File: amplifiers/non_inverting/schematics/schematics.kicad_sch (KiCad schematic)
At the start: 5 parts, among them J1 15V, U1 LM741

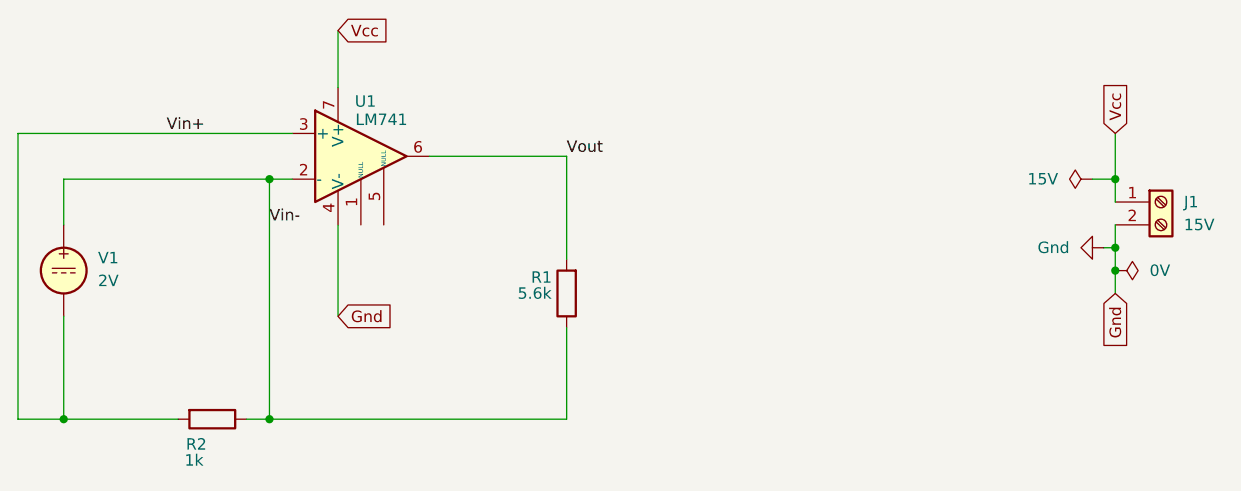
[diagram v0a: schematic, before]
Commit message: docs: update schematics.prl files for inverting and non-inverting amplifiers
Updated the schematics.prl files for both inverting and non-inverting
amplifiers to ensure proper referencing of all components and
connections. This update improves the accuracy of the schematic
representations and enhances the overall documentation quality.

Breaking changes: None

Resolves: None
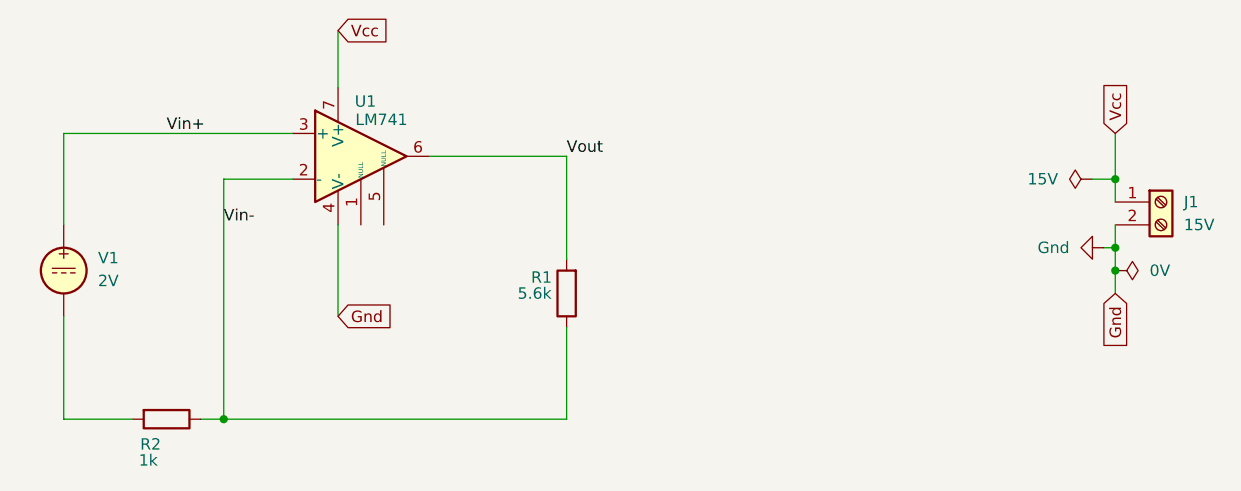
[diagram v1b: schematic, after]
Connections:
- net Vin+: now also V1.1; no longer R2.2, V1.2
- net Vin-: no longer V1.1
- new net: R2.2, V1.2
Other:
- moved on the sheet: R2
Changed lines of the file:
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@@
 	(paper "A5")
-	(junction
-		(at 43.18 33.02)
-		(diameter 0)
-		(color 0 0 0 0)
-	)
-	(junction
-		(at 20.32 59.69)
-		(diameter 0)
-		(color 0 0 0 0)
-	)
-	(junction
-		(at 43.18 59.69)
-		(diameter 0)
-		(color 0 0 0 0)
-	)
 	(junction
 		(at 137.16 33.02)
@@
 		(color 0 0 0 0)
 	)
+	(junction
+		(at 38.1 59.69)
+		(diameter 0)
+		(color 0 0 0 0)
+	)
 	(wire
 		(pts
@@
 	(wire
 		(pts
+			(xy 20.32 27.94) (xy 20.32 38.1)
+		)
+		(stroke
+			(width 0)
+			(type default)
+		)
+	)
+	(wire
+		(pts
 			(xy 50.8 48.26) (xy 50.8 38.1)
 		)
@@
 	(wire
 		(pts
-			(xy 15.24 59.69) (xy 20.32 59.69)
-		)
-		(stroke
-			(width 0)
-			(type default)
-		)
-	)
-	(wire
-		(pts
-			(xy 15.24 27.94) (xy 15.24 59.69)
-		)
-		(stroke
-			(width 0)
-			(type default)
-		)
-	)
-	(wire
-		(pts
 			(xy 137.16 43.18) (xy 137.16 45.72)
 		)
@@
 	(wire
 		(pts
-			(xy 43.18 59.69) (xy 76.2 59.69)
-		)
-		(stroke
-			(width 0)
-			(type default)
-		)
-	)
-	(wire
-		(pts
-			(xy 20.32 59.69) (xy 33.02 59.69)
-		)
-		(stroke
-			(width 0)
-			(type default)
-		)
-	)
-	(wire
-		(pts
-			(xy 43.18 33.02) (xy 45.72 33.02)
+			(xy 20.32 59.69) (xy 27.94 59.69)
+		)
+		(stroke
+			(width 0)
+			(type default)
+		)
+	)
+	(wire
+		(pts
+			(xy 38.1 33.02) (xy 45.72 33.02)
 		)
 		(stroke
@@
 	(wire
 		(pts
-			(xy 40.64 59.69) (xy 43.18 59.69)
-		)
-		(stroke
-			(width 0)
-			(type default)
-		)
-	)
-	(wire
-		(pts
-			(xy 20.32 33.02) (xy 43.18 33.02)
+			(xy 35.56 59.69) (xy 38.1 59.69)
 		)
 		(stroke
@@
 	(wire
 		(pts
-			(xy 45.72 27.94) (xy 15.24 27.94)
-		)
-		(stroke
-			(width 0)
-			(type default)
-		)
-	)
-	(wire
-		(pts
 			(xy 135.89 40.64) (xy 137.16 40.64)
 		)
@@
 	(wire
 		(pts
+			(xy 38.1 59.69) (xy 76.2 59.69)
+		)
+		(stroke
+			(width 0)
+			(type default)
+		)
+	)
+	(wire
+		(pts
 			(xy 60.96 30.48) (xy 76.2 30.48)
 		)
@@
 	(wire
 		(pts
-			(xy 20.32 38.1) (xy 20.32 33.02)
+			(xy 45.72 27.94) (xy 20.32 27.94)
 		)
 		(stroke
@@
 	(wire
 		(pts
-			(xy 43.18 59.69) (xy 43.18 33.02)
+			(xy 38.1 59.69) (xy 38.1 33.02)
 		)
 		(stroke
@@
 	)
 	(label "Vin-"
-		(at 43.18 38.1 0)
+		(at 38.1 38.1 0)
 		(effects
 			(font
@@
 	(symbol
 		(lib_id "Device:R")
-		(at 36.83 59.69 270)
+		(at 31.75 59.69 270)
 		(unit 1)
 		(exclude_from_sim no)
@@
 		(dnp no)
 		(property "Reference" "R2"
-			(at 35.052 62.484 90)
+			(at 29.972 62.484 90)
 			(effects
 				(font
@@
 		)
 		(property "Value" "1k"
-			(at 34.798 64.262 90)
+			(at 29.718 64.262 90)
 			(effects
 				(font
@@
 		)
 		(property "Footprint" ""
-			(at 36.83 57.912 90)
+			(at 31.75 57.912 90)
 			(effects
 				(font
@@
 		)
 		(property "Datasheet" "~"
-			(at 36.83 59.69 0)
+			(at 31.75 59.69 0)
 			(effects
 				(font
@@
 		)
 		(property "Description" "Resistor"
-			(at 36.83 59.69 0)
-			(effects
-				(font
+			(at 31.75 59.69 0)
+			(effects
+				(font
